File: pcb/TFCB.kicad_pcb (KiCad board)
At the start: 2 copper layers, 73 parts, among them J1 CONN_02X10, J10 PICKIT, J11 24V IN, J12 POWER, J2 CONN_02X10, J3 CONN_02X10, J4 CONN_02X10, J5 USB, J6 DB9, J7 SPI1, J8 SPI2, J9 RJ11 ICD, Q1 Q_PMOS_GDS, SW1 SW_PUSH, U1 REG-LM317, U2 REG-7805, U3 LD1086-3.3, U4 PIC-18F87J50-TQFP, U5 MAX3232_BJH, U6 LM431, U7 REF-LM4040, Y1 Crystal

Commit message: More work to TFCB
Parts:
- added G***: LOGO, bjh-kicad-logo-fp:logo_20mm_cu_hoskins_tech, F.Cu at (89.0, 71.0)
- J11: value 24V IN -> 24V
- J12: value POWER -> PSU
- moved R12 20.3 mm to (118.0, 98.5)
- moved J7 20.2 mm to (122.8, 98.5), turned to 270 degrees
- moved J8 20.0 mm to (122.7, 72.5), turned to 270 degrees
- moved R16 20.0 mm to (118.0, 72.5)
- moved J12 15.3 mm to (54.7, 137.3), turned to 90 degrees
- moved R15 13.0 mm to (118.0, 113.7)
- moved R19 10.5 mm to (118.0, 87.8)
- moved R13 10.1 mm to (118.0, 103.6)
- moved R17 9.89 mm to (118.1, 77.6)
- moved J11 4.71 mm to (110.5, 54.7), turned to 0 degrees
- moved C6 4.60 mm to (68.5, 138.0)
- moved C5 4.53 mm to (65.0, 138.0)
- moved C7 4.39 mm to (61.5, 138.0)
- moved R18 0.45 mm to (118.0, 82.7)
- moved R14 0.19 mm to (118.0, 108.7)
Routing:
- net GND: track 614.5 -> 558.6 mm, vias 5 -> 6
- net RB6: track 63.2 -> 83.6 mm
- net RB7: track 60.1 -> 78.0 mm
- net RF7: track 69.6 -> 87.1 mm
- net RC3: track 37.1 -> 25.2 mm
- net +5V: track 108.3 -> 118.8 mm
- net RC4: track 34.7 -> 27.6 mm
- net +14V: track 127.9 -> 134.0 mm, vias 0 -> 1
- net +3.3V: track 312.2 -> 306.3 mm
- net RD7: track 36.8 -> 41.6 mm, vias 0 -> 1
- net RC5: track 28.3 -> 25.1 mm
- net RD6: track 35.2 -> 32.9 mm
- net +24V: track 41.3 -> 39.5 mm
- net RD4: track 34.2 -> 35.8 mm
- net VDDCORE: track 29.7 -> 28.2 mm
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- added copper zone on B.Cu, net GND
- added copper zone on F.Cu, net GND
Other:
- net class Default: via_dia 1.27 -> 1.524
- net class Microcontroller: via_dia 1.27 -> 1.524
- board text added: "TFCB.Base Board August 2015 BJH"

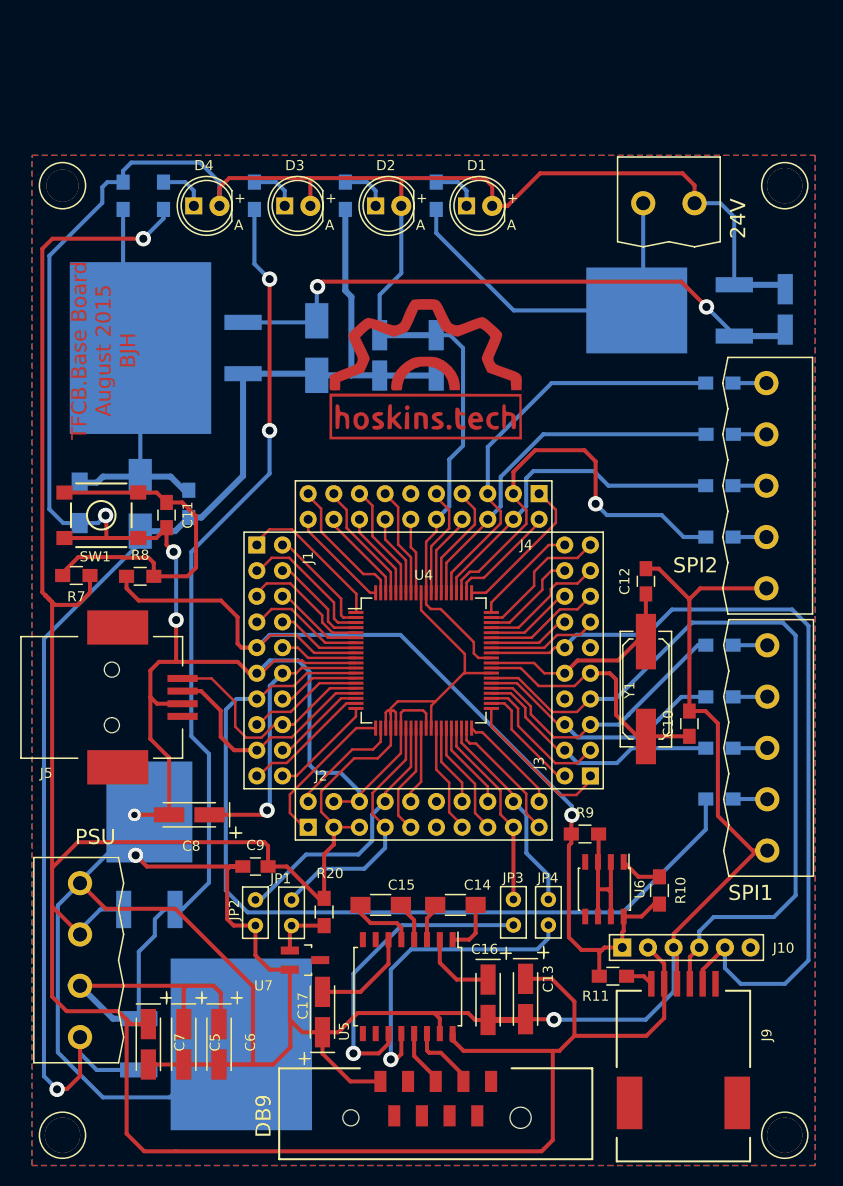
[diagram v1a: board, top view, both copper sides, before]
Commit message: Moved power regulators to top side and corrected bad package
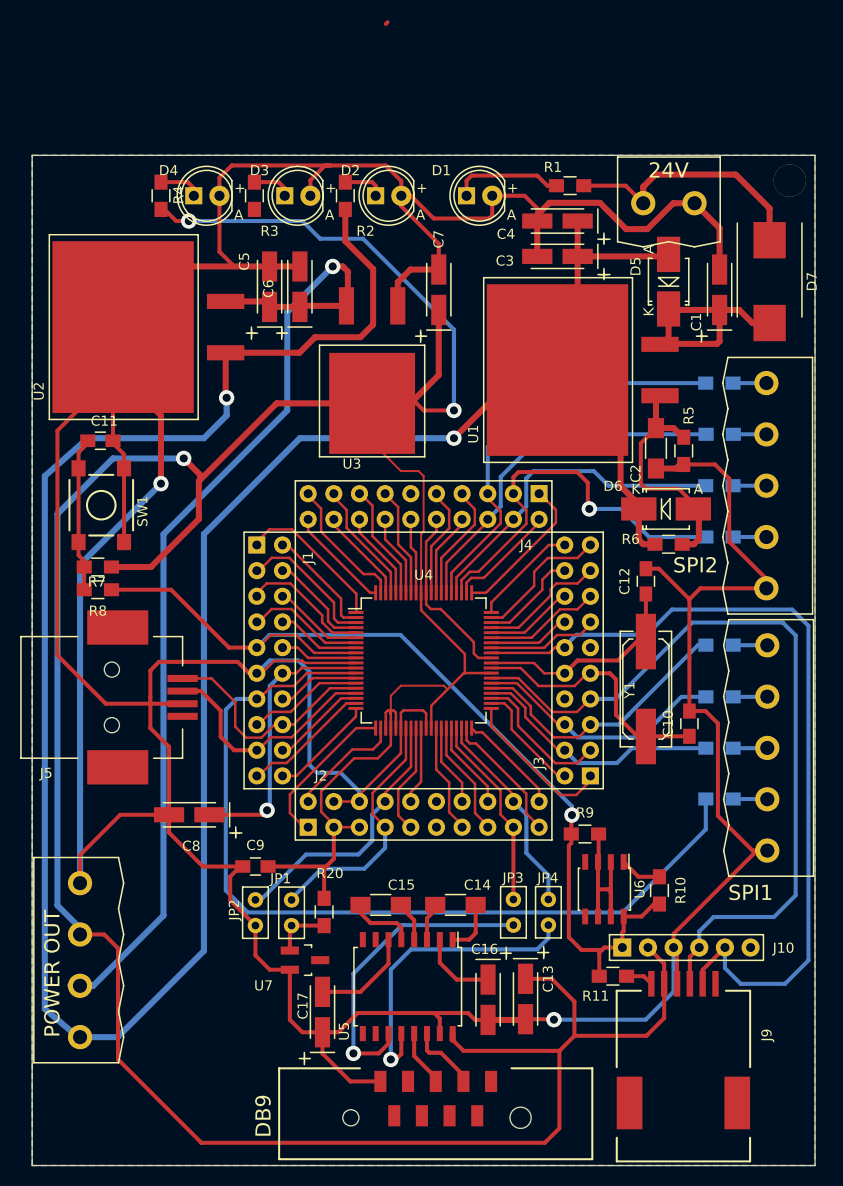
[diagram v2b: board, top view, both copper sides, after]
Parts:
- removed G***: LOGO, bjh-kicad-logo-fp:logo_20mm_cu_hoskins_tech
- removed Q1: Q_PMOS_GDS, bjh-kicad-transistor-fp:TO-263
- removed the REF** at (53.0, 147.0)
- removed the REF** at (124.5, 147.0)
- removed the REF** at (53.0, 53.0)
- removed the REF** at (124.5, 53.0)
- added D7: D, Diodes_SMD:DO-214AB_Handsoldering, F.Cu at (123.0, 62.5)
- added REF**: MountingHole_3-2mm, bjh-kicad-mountingholes-fp:MountingHole_3-2mm, F.Cu at (125.0, 52.5)
- C1, C2, C3, C4, D5, D6, R1, R2, R3, R4, R5, R6, U1, U2: moved to F.Cu
- J12: value PSU -> POWER OUT
- U3: value LD1086-3.3 -> REG-1086-3.3; moved to F.Cu
- moved C7 80.0 mm to (90.2, 63.3), turned to 90 degrees
- moved C5 75.5 mm to (73.5, 63.0), turned to 90 degrees
- moved C6 75.4 mm to (76.5, 63.0), turned to 90 degrees
- moved U2 72.1 mm to (71.0, 67.0)
- moved U3 67.2 mm to (83.7, 63.0)
- moved R5 61.0 mm to (114.5, 79.2), turned to 270 degrees
- moved C2 57.3 mm to (111.8, 79.0)
- moved D6 52.1 mm to (112.8, 85.0), turned to 180 degrees
- moved R6 47.7 mm to (113.0, 88.5), turned to 0 degrees
- moved U1 41.3 mm to (114.0, 71.2), turned to 90 degrees
- moved D5 35.4 mm to (113.0, 62.5), turned to 270 degrees
- moved C3 20.1 mm to (102.0, 60.0), turned to 180 degrees
- moved C4 17.9 mm to (102.0, 56.5), turned to 180 degrees
- moved R1 13.3 mm to (103.2, 53.0), turned to 180 degrees
- moved C11 9.85 mm to (56.8, 78.2), turned to 0 degrees
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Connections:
- net RA6 renamed OSC2
- U1 pad 1: Net-(C1-Pad1) -> Net-(C2-Pad1)
- U1 pad 2: Net-(C2-Pad1) -> +14V
- U1 pad 3: +14V -> Net-(C1-Pad1)
- U3 pad 1: +5V -> GND
- U3 pad 2: GND -> +3.3V
- U3 pad 3: +3.3V -> +5V
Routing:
- net +14V: track 134.0 -> 258.4 mm, vias 1 -> 2
- net +3.3V: track 306.3 -> 356.0 mm, vias 1 -> 3
- net Net-(C1-Pad1): track 60.8 -> 21.7 mm, vias 2 -> 0
- net GND: track 558.6 -> 534.4 mm, vias 6 -> 2
- net Net-(C11-Pad1): track 35.4 -> 15.4 mm
- net +5V: track 118.8 -> 102.2 mm, vias 2 -> 1
- net Net-(C2-Pad1): track 38.8 -> 24.3 mm
- net +24V: track 39.5 -> 25.8 mm
- net Net-(D1-Pad1): track 4.85 -> 11.0 mm
- net RD7: track 41.6 -> 38.5 mm
- net ~MCLR: track 96.8 -> 95.4 mm
- net Net-(D3-Pad1): track 4.85 -> 4.00 mm
- net Net-(D2-Pad1): track 4.85 -> 4.14 mm
- net Net-(D4-Pad1): track 4.85 -> 4.25 mm
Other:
- board outline added: 77.5 x 100 mm
- board text removed: "TFCB.Base Board August 2015 BJH"
